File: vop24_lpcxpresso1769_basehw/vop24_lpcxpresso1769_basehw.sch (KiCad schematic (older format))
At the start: 2 parts

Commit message: Primera versión esquematico sin revisar
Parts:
- gave numbers to parts that had none: 2
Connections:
- net labels added: BLE_EN, BLE_RXD, BLE_STATE, BLE_TXD, TPD_~ACK, TPD_~EN, USB_D+, USB_D-, USB_ID, UURXD, UUTXD, VUSB_OUT
- wire segments 45 -> 85
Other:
- note added: "P0.2-TXD0"
- note added: "P0.3-RXD0"
- moved on the sheet: J1, U1

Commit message: Algunas correcciones sobre el esquemático. Falta terminar de revisar algunos conflictos del DRC
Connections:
- wire segments 85 -> 86
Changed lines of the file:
@@
 F6 "USB_D-" B R 5050 3450 50
 F7 "USB_ID" B R 5050 3550 50
-F8 "USB_GND" B L 3350 3550 50
+F8 "USB_GND" B R 5050 4350 50
 F9 "VBAT-" B L 3350 2800 50
 F10 "VBAT+" B L 3350 2900 50
@@
 F21 "VCC_SW" B L 3350 3150 50
 F22 "GND_SW" B L 3350 3250 50
+F23 "LTC4411_STAT" I R 5050 4250 50
+F24 "S-S" I R 5050 4500 50
 $EndSheet
 Wire Wire Line
@@
 Text Label 7750 900  2    60   ~ 0
 DGND
+Wire Wire Line
+	10200 5400 10550 5400
+Text Label 10300 5400 0    50   ~ 0
+DGND
 $EndSCHEMATC

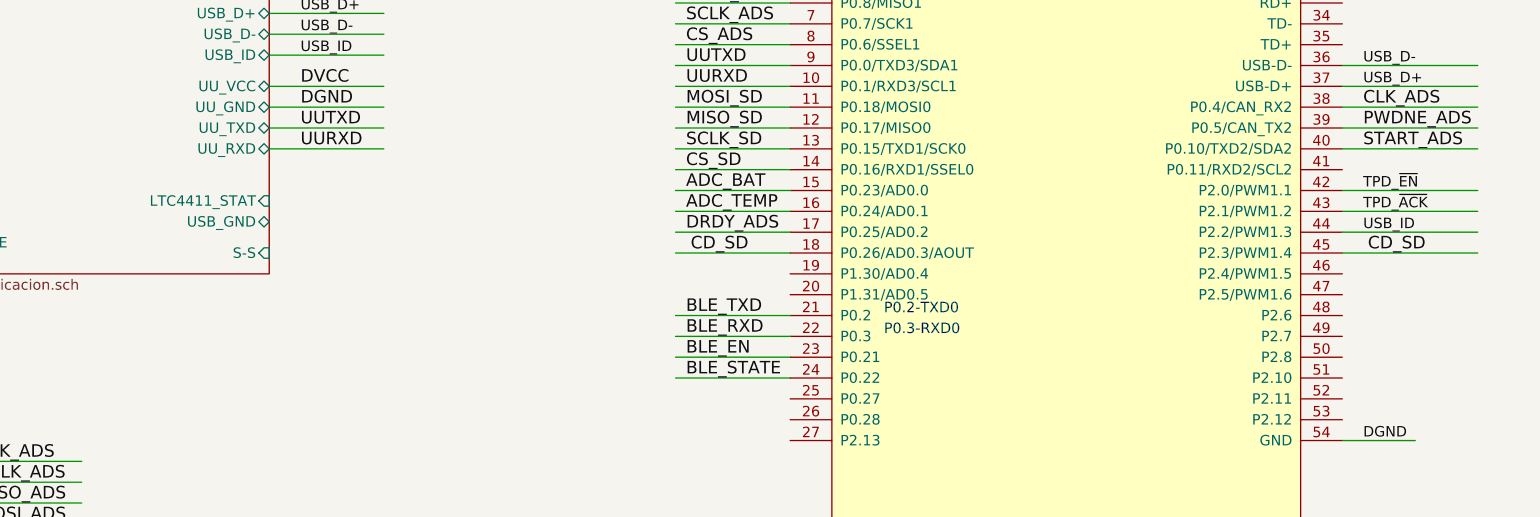
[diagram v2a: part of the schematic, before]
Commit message: Correcciones de esquemático:    - resueltos todos los conflictos de DRC    - cambio de circutio de medicion de temp    - ordenados todas las etiquetas y valores
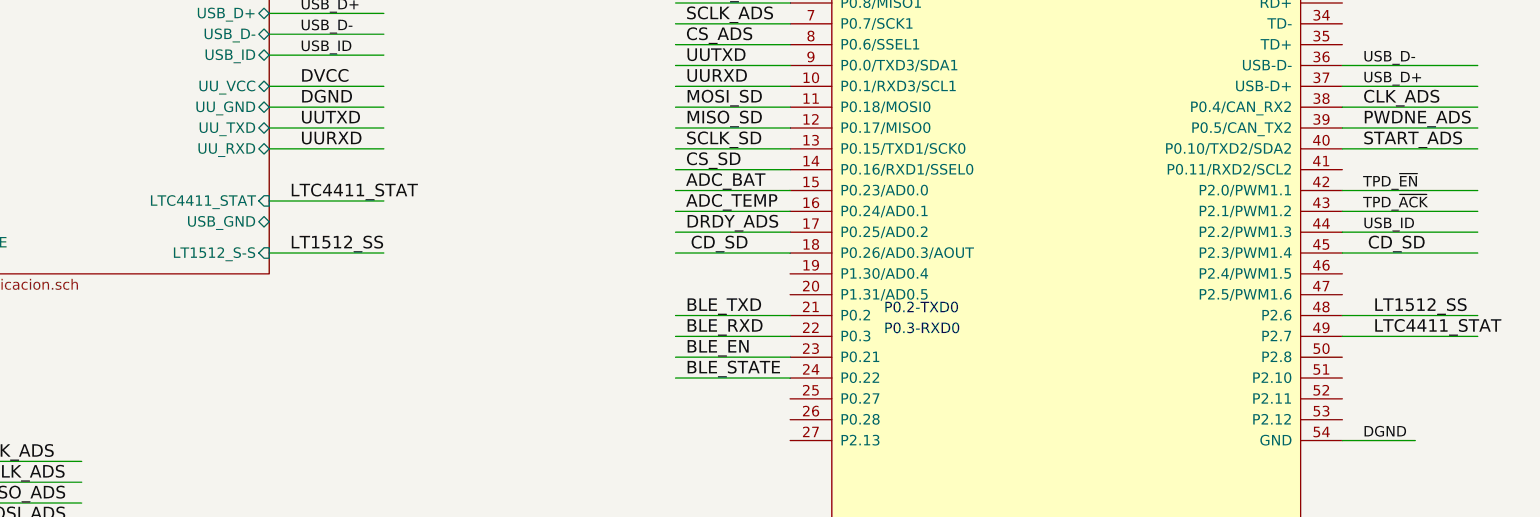
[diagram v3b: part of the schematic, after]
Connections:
- net labels added: LT1512_SS, LTC4411_STAT
- wire segments 86 -> 90
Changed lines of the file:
@@
 F22 "GND_SW" B L 3350 3250 50
 F23 "LTC4411_STAT" I R 5050 4250 50
-F24 "S-S" I R 5050 4500 50
+F24 "LT1512_S-S" I R 5050 4500 50
 $EndSheet
 Wire Wire Line
@@
 Text Label 10300 5400 0    50   ~ 0
 DGND
+Wire Wire Line
+	5050 4500 5600 4500
+Text Label 5150 4500 0    60   ~ 0
+LT1512_SS
+Wire Wire Line
+	10200 4800 10850 4800
+Text Label 10350 4800 0    60   ~ 0
+LT1512_SS
+Wire Wire Line
+	5050 4250 5600 4250
+Text Label 5150 4250 0    60   ~ 0
+LTC4411_STAT
+Wire Wire Line
+	10200 4900 10850 4900
+Text Label 10350 4900 0    60   ~ 0
+LTC4411_STAT
 $EndSCHEMATC

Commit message: Se agregaron la mayoría de los footprints de los ICs
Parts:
- J1: footprint (none) -> meport_kicad_libs:microSD_3020-901-0001-ACH-ELECTRONICS
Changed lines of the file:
@@
 F 0 "J1" H 8050 2100 50  0000 C CNN
 F 1 "Micro_SD_Card" H 9350 2100 50  0000 R CNN
-F 2 "" H 9850 1800 50  0001 C CNN
+F 2 "meport_kicad_libs:microSD_3020-901-0001-ACH-ELECTRONICS" H 9850 1800 50  0001 C CNN
 F 3 "" H 8700 1500 50  0001 C CNN
 	1    8700 1500

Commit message: Finalizada asociación de todos los footprints. Ver librerías froux-kicad
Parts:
- U1: footprint (none) -> meport_kicad_libs:LPCXpresso1769
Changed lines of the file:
@@
 F 0 "U1" H 7800 6050 60  0000 C CNN
 F 1 "LPCXpresso1769" H 8100 6150 60  0000 C CNN
-F 2 "" H 8600 4750 60  0001 C CNN
+F 2 "meport_kicad_libs:LPCXpresso1769" H 8600 4750 60  0001 C CNN
 F 3 "" H 8600 4750 60  0001 C CNN
 	1    8900 4350

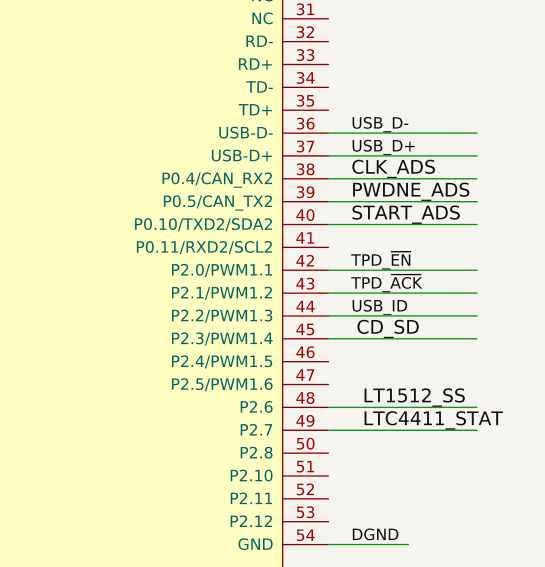
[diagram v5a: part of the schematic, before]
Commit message: Primer commit sobre el diseño del PCB. Se agruparon algunas hojas de esquemáticos. No se empezó a rutear
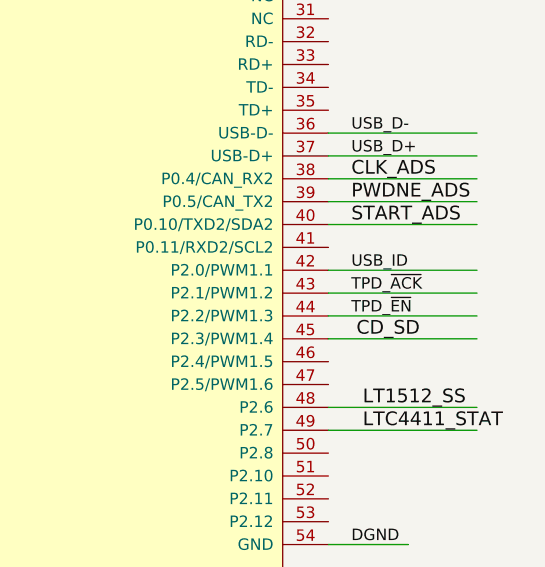
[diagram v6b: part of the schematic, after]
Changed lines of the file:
@@
 Wire Wire Line
 	10200 4300 10850 4300
-Text Label 10300 4200 0    50   ~ 0
+Text Label 10300 4400 0    50   ~ 0
 TPD_~EN
 Text Label 10300 4300 0    50   ~ 0
@@
 Wire Wire Line
 	10200 4400 10850 4400
-Text Label 10300 4400 0    50   ~ 0
+Text Label 10300 4200 0    50   ~ 0
 USB_ID
 $Sheet

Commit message: PCB: primera versión de ruteo finalizado sin poligonos. SCH: cambios de conexiones para facilitar conexiones
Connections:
- wire segments 90 -> 91
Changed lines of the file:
@@
 Wire Wire Line
 	7000 5100 7550 5100
-Text Label 7050 5000 0    60   ~ 0
-BLE_EN
 Text Label 7050 5100 0    60   ~ 0
 BLE_STATE
@@
 Text Label 10350 4900 0    60   ~ 0
 LTC4411_STAT
-Text Label 10600 4500 2    60   ~ 0
-CD_SD
+Wire Wire Line
+	7550 4700 7000 4700
+Text Label 7050 4700 0    60   ~ 0
+BLE_EN
 $EndSCHEMATC
